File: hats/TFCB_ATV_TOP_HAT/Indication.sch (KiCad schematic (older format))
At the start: 4 parts

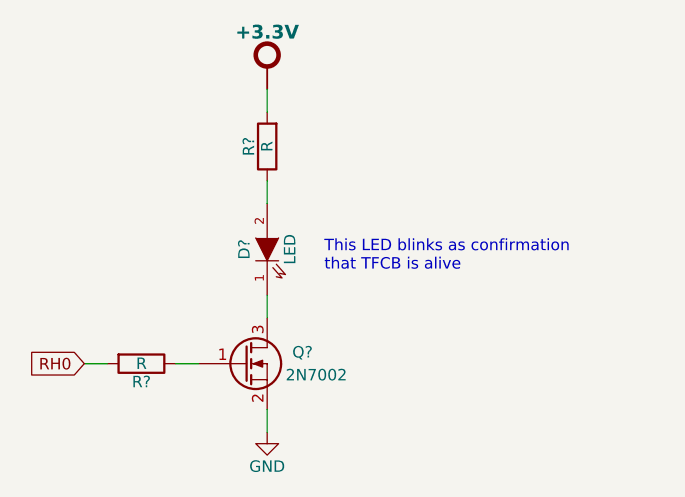
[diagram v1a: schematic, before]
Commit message: Added scanner trigger and current sense cct
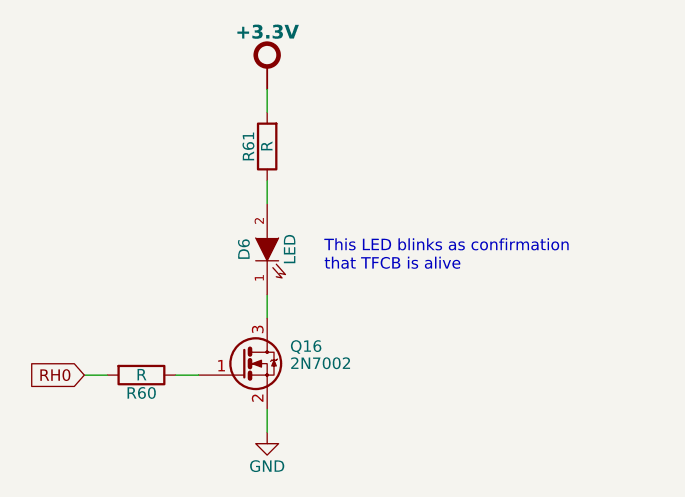
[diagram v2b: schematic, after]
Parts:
- removed Q?: 2N7002, symbol Q_NMOS_GSD
- added Q16: 2N7002, Housings_SOT-23_SOT-143_TSOT-6:SOT-23, symbol 2N7002
- D6: renamed from D?; footprint (none) -> LEDs:LED-1206
- R60, R61: renamed from R?; footprint (none) -> Resistors_SMD:R_0805_HandSoldering
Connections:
- net GND: now also Q16.2 (S)
- net at R60.1: now also Q16.1 (G)
- net at D6.1 (K): now also Q16.3 (D)
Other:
- moved on the sheet: R60
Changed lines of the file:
@@
 LIBS:contrib
 LIBS:valves
+LIBS:buzzer
+LIBS:Relays
+LIBS:PowerSymbols-BJH
+LIBS:Oscillators-BJH
+LIBS:Microchip-BJH
+LIBS:LCD-BJH
+LIBS:Devices-BJH
+LIBS:Connectors-BJH
 LIBS:Basics-BJH
-LIBS:buzzer
-LIBS:Connectors-BJH
-LIBS:Devices-BJH
-LIBS:LCD-BJH
-LIBS:Microchip-BJH
-LIBS:Oscillators-BJH
-LIBS:PowerSymbols-BJH
-LIBS:Relays
+LIBS:Transistors-BJH
 LIBS:TFCB_ATV_HAT-cache
 EELAYER 25 0
@@
 $Descr A4 11693 8268
 encoding utf-8
-Sheet 6 7
+Sheet 6 6
 Title "Indication"
 Date ""
@@
 Comment4 ""
 $EndDescr
-$Comp
-L Q_NMOS_GSD Q?
-U 1 1 55A3B534
-P 1850 2200
-F 0 "Q?" H 2150 2250 50  0000 R CNN
-F 1 "2N7002" H 2300 2150 50  0000 R CNN
-F 2 "" H 2050 2300 29  0000 C CNN
-F 3 "" H 1850 2200 60  0000 C CNN
-	1    1850 2200
-	1    0    0    -1
-$EndComp
-Text GLabel 1150 2200 0    50   Input ~ 0
+Text GLabel 1150 2250 0    50   Input ~ 0
 RH0
 $Comp
-L R R?
+L R R60
 U 1 1 55A3B59B
-P 1400 2200
-F 0 "R?" V 1480 2200 50  0000 C CNN
-F 1 "R" V 1400 2200 50  0000 C CNN
-F 2 "" V 1330 2200 30  0000 C CNN
-F 3 "" H 1400 2200 30  0000 C CNN
-	1    1400 2200
+P 1400 2250
+F 0 "R60" V 1480 2250 50  0000 C CNN
+F 1 "R" V 1400 2250 50  0000 C CNN
+F 2 "Resistors_SMD:R_0805_HandSoldering" V 1330 2250 30  0001 C CNN
+F 3 "" H 1400 2250 30  0000 C CNN
+	1    1400 2250
 	0    1    1    0
 $EndComp
 Wire Wire Line
-	1150 2200 1250 2200
+	1150 2250 1250 2250
 Wire Wire Line
-	1550 2200 1650 2200
+	1550 2250 1650 2250
 $Comp
-L LED D?
+L LED D6
 U 1 1 55A3B63F
 P 1950 1700
-F 0 "D?" H 1950 1800 50  0000 C CNN
+F 0 "D6" H 1950 1800 50  0000 C CNN
 F 1 "LED" H 1950 1600 50  0000 C CNN
-F 2 "" H 1950 1700 60  0000 C CNN
+F 2 "LEDs:LED-1206" H 1950 1700 60  0001 C CNN
 F 3 "" H 1950 1700 60  0000 C CNN
 	1    1950 1700
@@
 	1950 1900 1950 2000
 $Comp
-L R R?
+L R R61
 U 1 1 55A3B688
 P 1950 1250
-F 0 "R?" V 2030 1250 50  0000 C CNN
+F 0 "R61" V 2030 1250 50  0000 C CNN
 F 1 "R" V 1950 1250 50  0000 C CNN
-F 2 "" V 1880 1250 30  0000 C CNN
+F 2 "Resistors_SMD:R_0805_HandSoldering" V 1880 1250 30  0001 C CNN
 F 3 "" H 1950 1250 30  0000 C CNN
 	1    1950 1250
@@
 $EndComp
 $Comp
-L +3.3V_BJH #PWR?
+L +3.3V_BJH #PWR087
 U 1 1 55A3B6D8
 P 1950 950
-F 0 "#PWR?" H 1950 1140 20  0001 C CNN
+F 0 "#PWR087" H 1950 1140 20  0001 C CNN
 F 1 "+3.3V_BJH" H 1950 1140 51  0001 C CNN
 F 2 "" H 1950 950 60  0001 C CNN
@@
 $EndComp
 $Comp
-L GND #PWR?
+L GND #PWR088
 U 1 1 55A3B707
 P 1950 2500
-F 0 "#PWR?" H 1950 2250 50  0001 C CNN
+F 0 "#PWR088" H 1950 2250 50  0001 C CNN
 F 1 "GND" H 1950 2350 50  0000 C CNN
 F 2 "" H 1950 2500 60  0000 C CNN
@@
 Text Notes 2200 1800 0    50   ~ 0
 This LED blinks as confirmation\nthat TFCB is alive
+$Comp
+L 2N7002 Q16
+U 1 1 55B12C45
+P 1850 2200
+F 0 "Q16" H 2050 2275 50  0000 L CNN
+F 1 "2N7002" H 2050 2200 50  0000 L CNN
+F 2 "Housings_SOT-23_SOT-143_TSOT-6:SOT-23" H 2050 2125 50  0001 L CIN
+F 3 "" H 1850 2200 50  0000 L CNN
+	1    1850 2200
+	1    0    0    -1
+$EndComp
 $EndSCHEMATC
